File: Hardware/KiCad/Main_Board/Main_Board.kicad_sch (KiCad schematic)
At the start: 0 parts

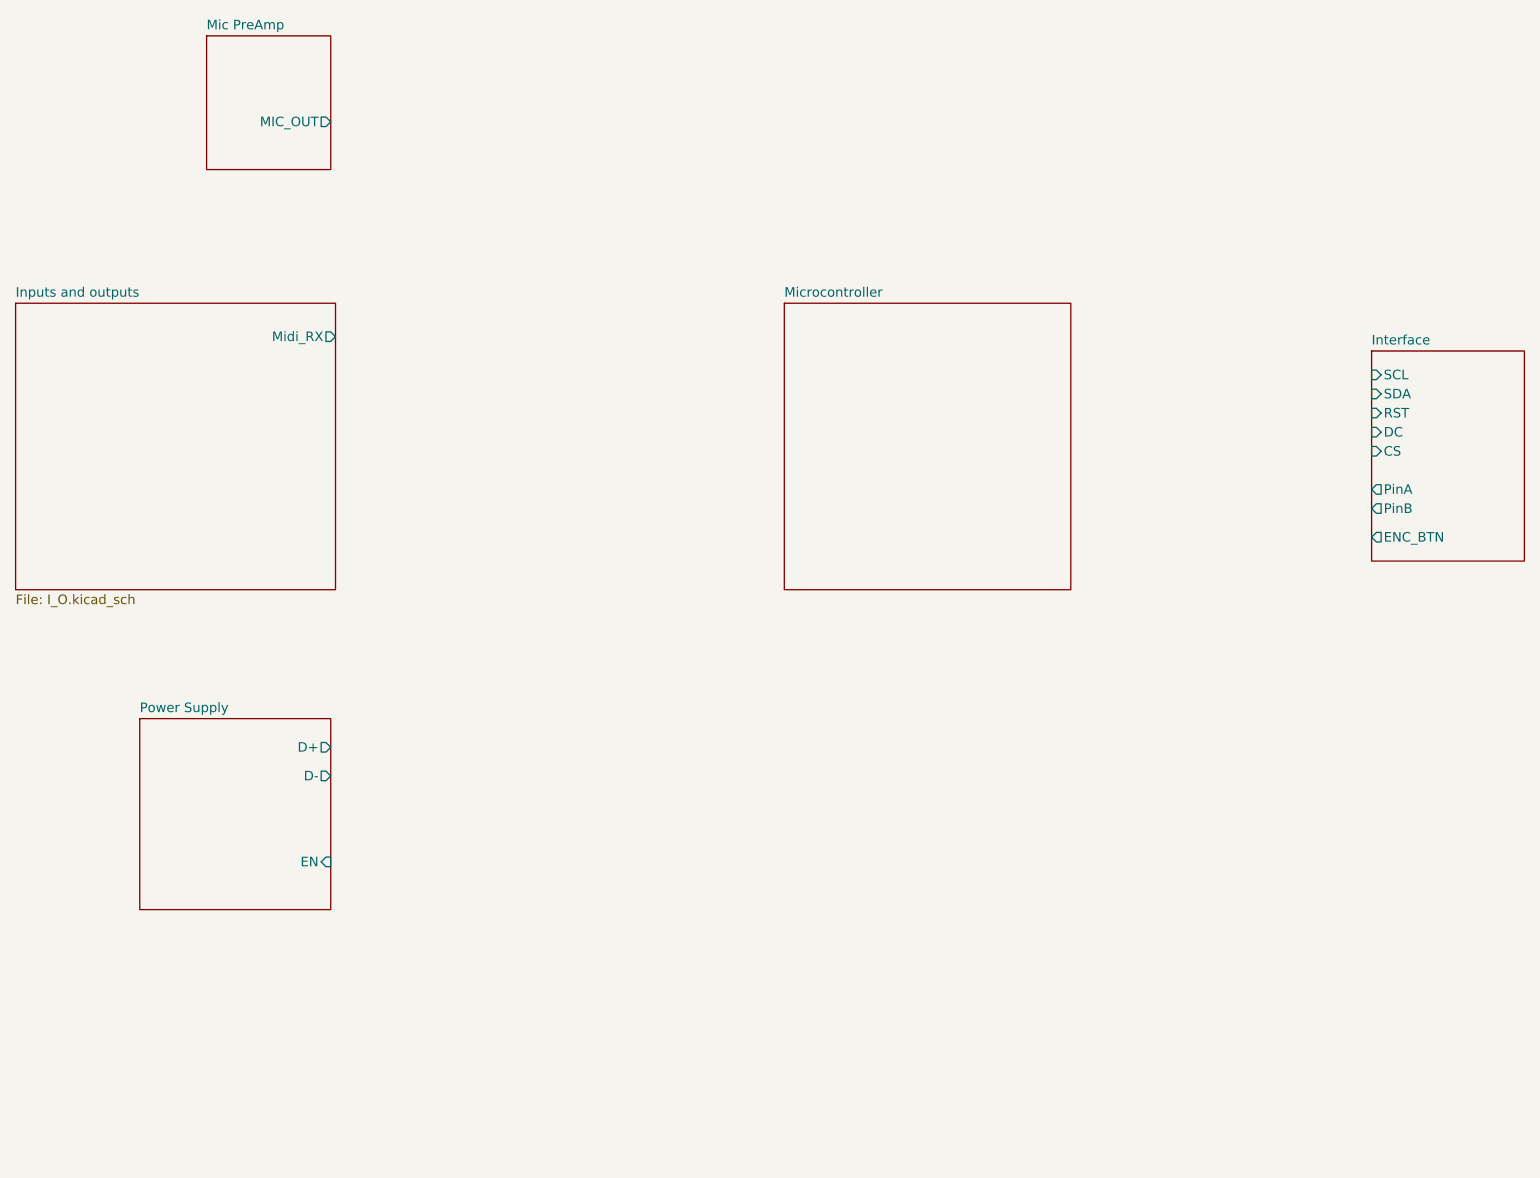
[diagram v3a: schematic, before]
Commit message: Connected screen, USB and encoder in the main sheet
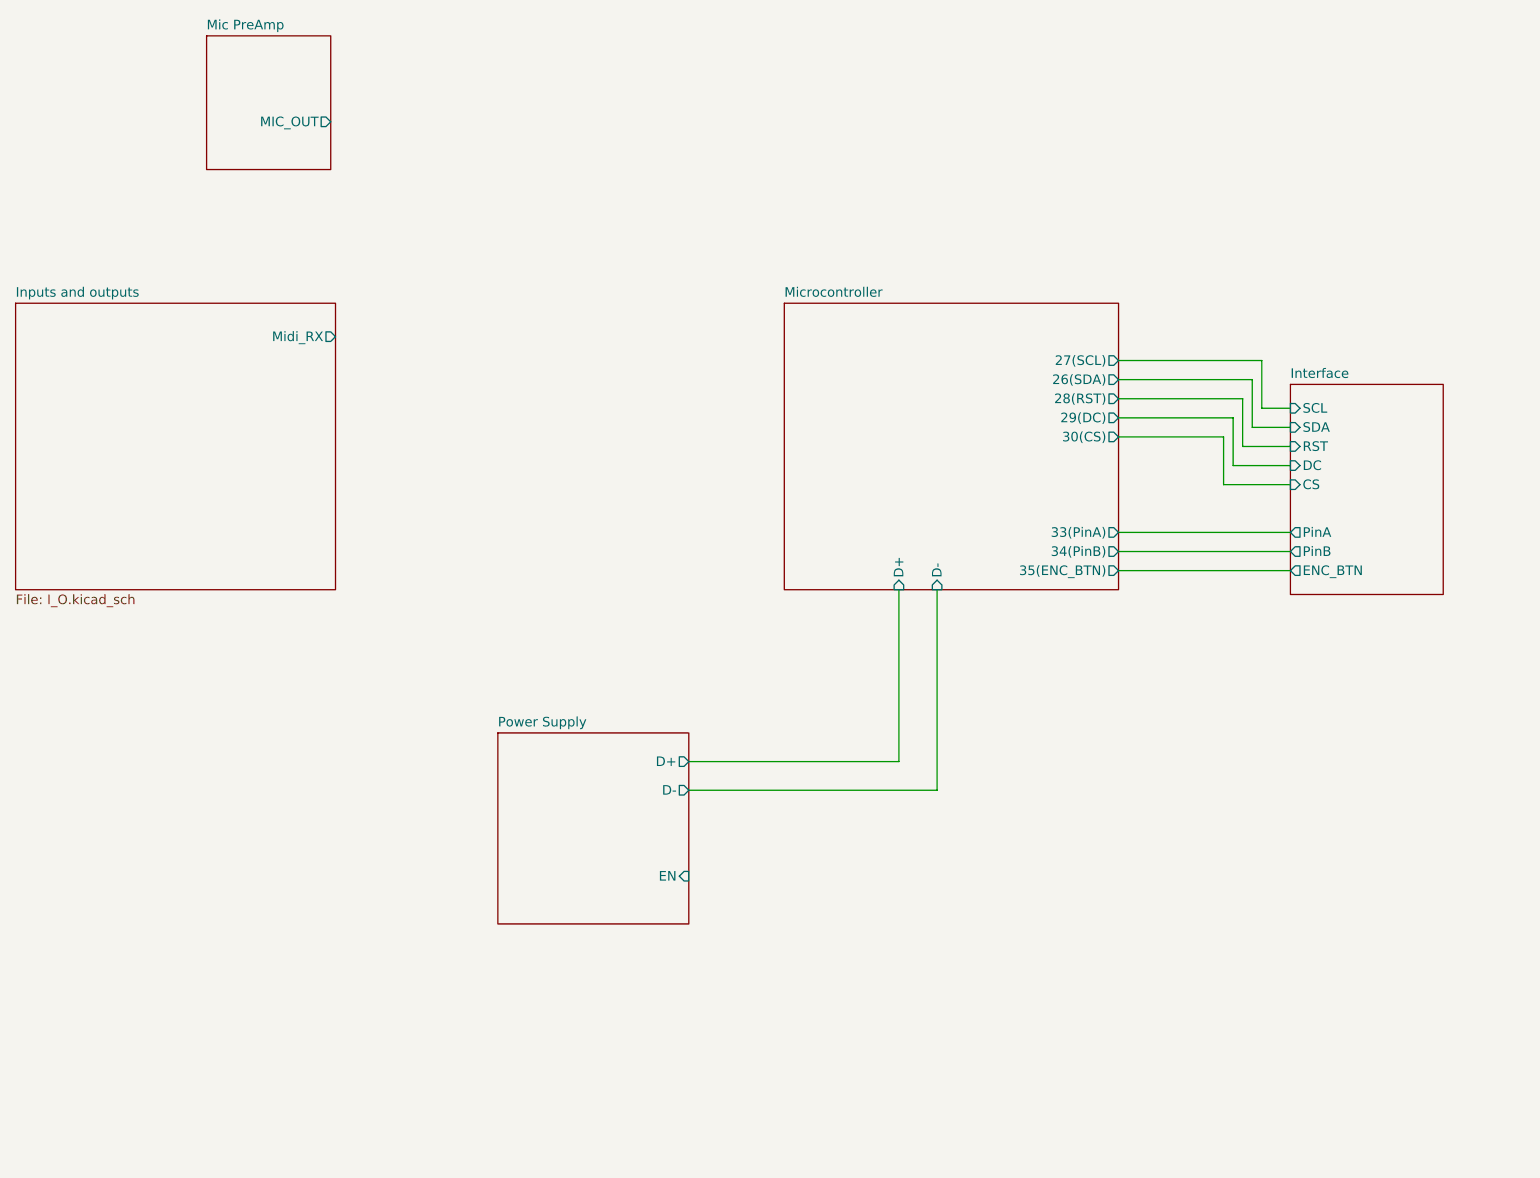
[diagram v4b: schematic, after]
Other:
- sheet Microcontroller ports: added 26(SDA), 27(SCL), 28(RST), 29(DC), 30(CS), 33(PinA), 34(PinB), 35(ENC_BTN), D+, D-; removed none
